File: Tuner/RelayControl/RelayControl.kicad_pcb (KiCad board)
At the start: 2 copper layers, 100 x 100 mm, 138 parts, among them J1 Conn_01x06, J12 Conn_01x01, J13 Conn_01x01, J14 Conn_01x01, J15 Conn_01x01, J2 Conn_02x16_Odd_Even, J3 Conn_01x06, J4 Conn_02x16_Odd_Even, J5 Conn_01x01, J6 Conn_01x01, J7 Conn_01x01, J8 Conn_01x01, U1 MCP23017, U2 ULN2803A, U3 ULN2803A, U4 MCP23017, U5 ULN2803A, U6 ULN2803A

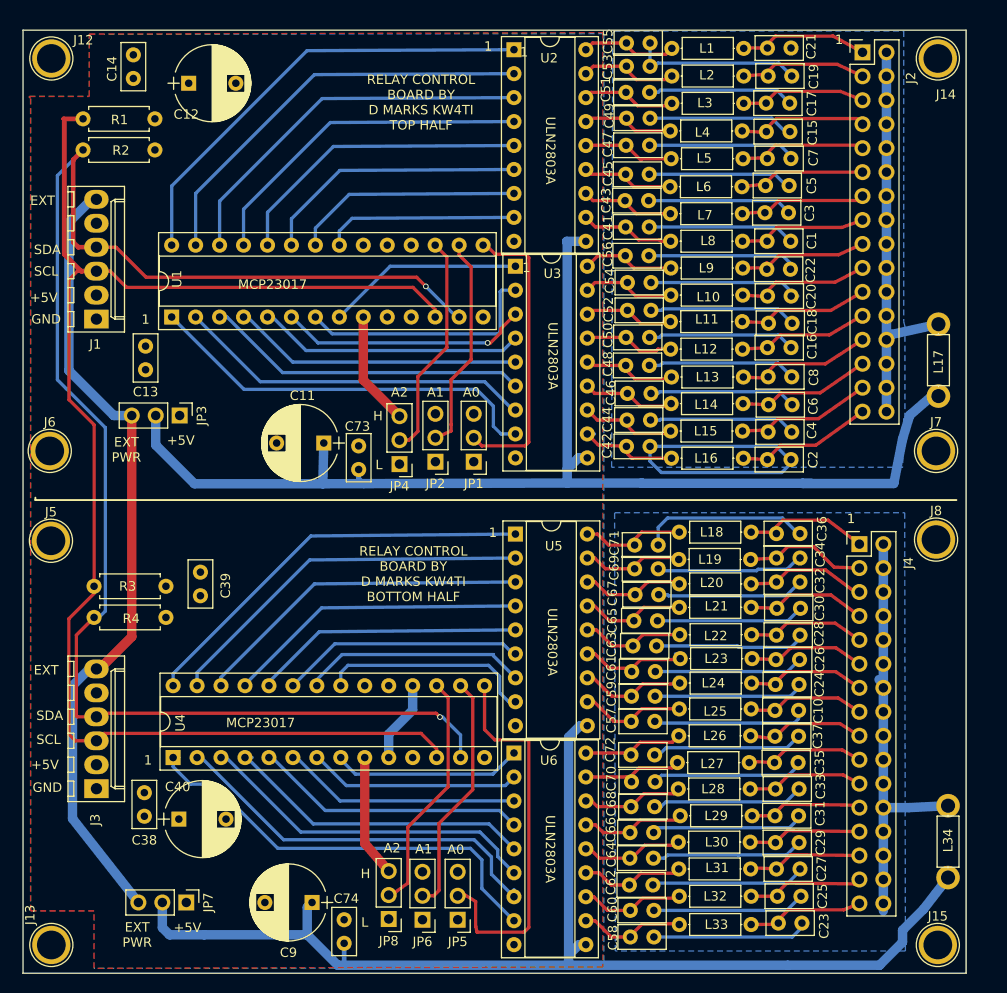
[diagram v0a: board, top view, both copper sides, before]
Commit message: Modified RelayControl and Reversible Section to Isolate Digital from Analog sections using RF chokes
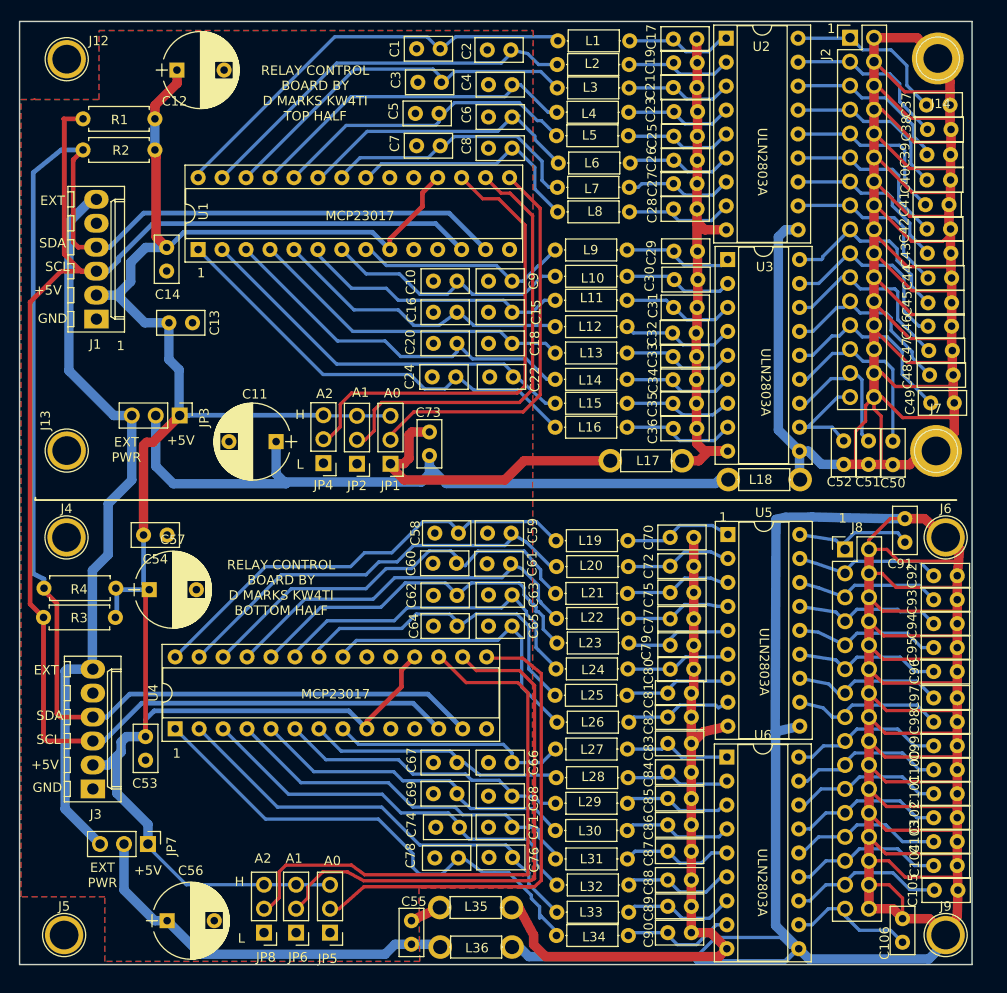
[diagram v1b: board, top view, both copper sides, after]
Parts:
- removed J15: Conn_01x01, Connectors:1pin
- added C100: 10 nF, Capacitors_THT:C_Disc_D5.0mm_W2.5mm_P2.50mm, F.Cu at (146.6, 128.4)
- added C101: 10 nF, Capacitors_THT:C_Disc_D5.0mm_W2.5mm_P2.50mm, F.Cu at (146.6, 131.0)
- added C102: 10 nF, Capacitors_THT:C_Disc_D5.0mm_W2.5mm_P2.50mm, F.Cu at (146.6, 133.5)
- added C103: 10 nF, Capacitors_THT:C_Disc_D5.0mm_W2.5mm_P2.50mm, F.Cu at (146.6, 136.0)
- added C104: 10 nF, Capacitors_THT:C_Disc_D5.0mm_W2.5mm_P2.50mm, F.Cu at (146.6, 138.6)
- added C105: 10 nF, Capacitors_THT:C_Disc_D5.0mm_W2.5mm_P2.50mm, F.Cu at (146.6, 141.2)
- added C106: 10 nF, Capacitors_THT:C_Disc_D5.0mm_W2.5mm_P2.50mm, F.Cu at (143.3, 146.7)
- added C75: 10 nF, Capacitors_THT:C_Disc_D5.0mm_W2.5mm_P2.50mm, F.Cu at (118.6, 109.6)
- added C76: 10 nF, Capacitors_THT:C_Disc_D5.0mm_W2.5mm_P2.50mm, F.Cu at (101.9, 137.7)
- added C77: 10 nF, Capacitors_THT:C_Disc_D5.0mm_W2.5mm_P2.50mm, F.Cu at (118.6, 112.4)
- added C78: 10 nF, Capacitors_THT:C_Disc_D5.0mm_W2.5mm_P2.50mm, F.Cu at (96.2, 137.8)
- added C79: 10 nF, Capacitors_THT:C_Disc_D5.0mm_W2.5mm_P2.50mm, F.Cu at (118.6, 115.2)
- added C80: 10 nF, Capacitors_THT:C_Disc_D5.0mm_W2.5mm_P2.50mm, F.Cu at (118.6, 117.8)
- added C81: 10 nF, Capacitors_THT:C_Disc_D5.0mm_W2.5mm_P2.50mm, F.Cu at (118.4, 120.3)
- added C82: 10 nF, Capacitors_THT:C_Disc_D5.0mm_W2.5mm_P2.50mm, F.Cu at (118.4, 122.8)
- added C83: 10 nF, Capacitors_THT:C_Disc_D5.0mm_W2.5mm_P2.50mm, F.Cu at (118.4, 125.6)
- added C84: 10 nF, Capacitors_THT:C_Disc_D5.0mm_W2.5mm_P2.50mm, F.Cu at (118.4, 128.7)
- added C85: 10 nF, Capacitors_THT:C_Disc_D5.0mm_W2.5mm_P2.50mm, F.Cu at (118.4, 131.5)
- added C86: 10 nF, Capacitors_THT:C_Disc_D5.0mm_W2.5mm_P2.50mm, F.Cu at (118.4, 134.3)
- added C87: 10 nF, Capacitors_THT:C_Disc_D5.0mm_W2.5mm_P2.50mm, F.Cu at (118.4, 137.1)
- added C88: 10 nF, Capacitors_THT:C_Disc_D5.0mm_W2.5mm_P2.50mm, F.Cu at (118.4, 140.1)
- added C89: 10 nF, Capacitors_THT:C_Disc_D5.0mm_W2.5mm_P2.50mm, F.Cu at (118.4, 142.9)
- added C90: 10 nF, Capacitors_THT:C_Disc_D5.0mm_W2.5mm_P2.50mm, F.Cu at (118.4, 145.7)
- added C91: 10 nF, Capacitors_THT:C_Disc_D5.0mm_W2.5mm_P2.50mm, F.Cu at (143.5, 104.3)
- added C92: 10 nF, Capacitors_THT:C_Disc_D5.0mm_W2.5mm_P2.50mm, F.Cu at (146.6, 107.8)
- added C93: 10 nF, Capacitors_THT:C_Disc_D5.0mm_W2.5mm_P2.50mm, F.Cu at (146.6, 110.4)
- added C94: 10 nF, Capacitors_THT:C_Disc_D5.0mm_W2.5mm_P2.50mm, F.Cu at (146.6, 112.9)
- added C95: 10 nF, Capacitors_THT:C_Disc_D5.0mm_W2.5mm_P2.50mm, F.Cu at (146.6, 115.5)
- added C96: 10 nF, Capacitors_THT:C_Disc_D5.0mm_W2.5mm_P2.50mm, F.Cu at (146.6, 118.0)
- added C97: 10 nF, Capacitors_THT:C_Disc_D5.0mm_W2.5mm_P2.50mm, F.Cu at (146.6, 120.8)
- added C98: 10 nF, Capacitors_THT:C_Disc_D5.0mm_W2.5mm_P2.50mm, F.Cu at (146.6, 123.3)
- added C99: 10 nF, Capacitors_THT:C_Disc_D5.0mm_W2.5mm_P2.50mm, F.Cu at (146.6, 125.9)
- added J9: Conn_01x01, Connectors:1pin, F.Cu at (147.8, 145.9)
- added L35: 100 uH, Inductors_THT:L_Axial_L5.3mm_D2.2mm_P7.62mm_Horizontal_Vishay_IM-1, F.Cu at (94.2, 143.0)
- added L36: 100 uH, Inductors_THT:L_Axial_L5.3mm_D2.2mm_P7.62mm_Horizontal_Vishay_IM-1, F.Cu at (101.9, 147.2)
- C38, C39, C74: value 100 nF -> 10 nF
- C40, C9: value 100 uF -> 10 nF; footprint Capacitors_THT:CP_Radial_D8.0mm_P5.00mm -> Capacitors_THT:C_Disc_D5.0mm_W2.5mm_P2.50mm
- C53, C54, C55: value 10 nF -> 100 nF
- C56, C57: value 10 nF -> 100 uF; footprint Capacitors_THT:C_Disc_D5.0mm_W2.5mm_P2.50mm -> Capacitors_THT:CP_Radial_D8.0mm_P5.00mm
- J4: value Conn_02x16_Odd_Even -> Conn_01x01; footprint Pin_Headers:Pin_Header_Straight_2x16_Pitch2.54mm -> Connectors:1pin
- J8: value Conn_01x01 -> Conn_02x16_Odd_Even; footprint Connectors:1pin -> Pin_Headers:Pin_Header_Straight_2x16_Pitch2.54mm
- moved C38 110.4 mm to (145.9, 60.5), turned to 0 degrees
- moved C40 104.3 mm to (145.8, 65.9)
- moved C55 96.4 mm to (91.2, 144.4), turned to 270 degrees
- moved J6 95.4 mm to (147.8, 103.8)
- moved C53 91.0 mm to (63.0, 127.4), turned to 90 degrees
- moved C39 90.1 mm to (145.8, 63.2), turned to 0 degrees
- moved C23 87.1 mm to (119.0, 58.6), turned to 0 degrees
- moved C56 87.1 mm to (65.3, 144.4), turned to 0 degrees
- moved J4 84.1 mm to (54.6, 103.8)
- moved C25 81.7 mm to (119.0, 61.2), turned to 0 degrees
- moved C27 73.9 mm to (119.0, 66.3), turned to 0 degrees
- moved C9 69.2 mm to (101.9, 76.6)
- moved C37 68.3 mm to (145.8, 57.9), turned to 0 degrees
- moved C29 64.1 mm to (119.0, 73.4), turned to 0 degrees
- moved C10 58.2 mm to (96.0, 76.6)
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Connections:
- C1 pad 2: Net-(C1-Pad2) -> GND
- C10 pad 2: Net-(C10-Pad2) -> GND
- C15 pad 1: Net-(C1-Pad1) -> Net-(C15-Pad1)
- C15 pad 2: Net-(C15-Pad2) -> GND
- C16 pad 1: Net-(C1-Pad1) -> Net-(C16-Pad1)
- C16 pad 2: Net-(C16-Pad2) -> GND
- C17 pad 1: Net-(C1-Pad1) -> Net-(C17-Pad1)
- C18 pad 1: Net-(C1-Pad1) -> Net-(C18-Pad1)
- C18 pad 2: Net-(C18-Pad2) -> GND
- C19 pad 1: Net-(C1-Pad1) -> Net-(C19-Pad1)
- C19 pad 2: Net-(C19-Pad2) -> Net-(C17-Pad2)
- C2 pad 1: Net-(C1-Pad1) -> Net-(C2-Pad1)
- C2 pad 2: Net-(C2-Pad2) -> GND
- C20 pad 1: Net-(C1-Pad1) -> Net-(C20-Pad1)
- C20 pad 2: Net-(C20-Pad2) -> GND
- C21 pad 1: Net-(C1-Pad1) -> Net-(C21-Pad1)
- C21 pad 2: Net-(C21-Pad2) -> Net-(C17-Pad2)
- C22 pad 1: Net-(C1-Pad1) -> Net-(C22-Pad1)
- C22 pad 2: Net-(C22-Pad2) -> GND
- C23 pad 1: Net-(C10-Pad1) -> Net-(C23-Pad1)
- C23 pad 2: Net-(C23-Pad2) -> Net-(C17-Pad2)
- C24 pad 1: Net-(C10-Pad1) -> Net-(C24-Pad1)
- C24 pad 2: Net-(C24-Pad2) -> GND
- C25 pad 1: Net-(C10-Pad1) -> Net-(C25-Pad1)
- C25 pad 2: Net-(C25-Pad2) -> Net-(C17-Pad2)
- C26 pad 1: Net-(C10-Pad1) -> Net-(C26-Pad1)
- C26 pad 2: Net-(C26-Pad2) -> Net-(C17-Pad2)
- C27 pad 1: Net-(C10-Pad1) -> Net-(C27-Pad1)
- C27 pad 2: Net-(C27-Pad2) -> Net-(C17-Pad2)
- C28 pad 1: Net-(C10-Pad1) -> Net-(C28-Pad1)
- C28 pad 2: Net-(C28-Pad2) -> Net-(C17-Pad2)
- C29 pad 1: Net-(C10-Pad1) -> Net-(C29-Pad1)
- C29 pad 2: Net-(C29-Pad2) -> Net-(C17-Pad2)
- C3 pad 1: Net-(C1-Pad1) -> Net-(C3-Pad1)
- C3 pad 2: Net-(C3-Pad2) -> GND
- C30 pad 1: Net-(C10-Pad1) -> Net-(C30-Pad1)
- C30 pad 2: Net-(C30-Pad2) -> Net-(C17-Pad2)
- C31 pad 1: Net-(C10-Pad1) -> Net-(C31-Pad1)
- C31 pad 2: Net-(C31-Pad2) -> Net-(C17-Pad2)
- C32 pad 1: Net-(C10-Pad1) -> Net-(C32-Pad1)
- C32 pad 2: Net-(C32-Pad2) -> Net-(C17-Pad2)
- C33 pad 1: Net-(C10-Pad1) -> Net-(C33-Pad1)
- C33 pad 2: Net-(C33-Pad2) -> Net-(C17-Pad2)
- C34 pad 1: Net-(C10-Pad1) -> Net-(C34-Pad1)
- C34 pad 2: Net-(C34-Pad2) -> Net-(C17-Pad2)
- C35 pad 1: Net-(C10-Pad1) -> Net-(C35-Pad1)
- C35 pad 2: Net-(C35-Pad2) -> Net-(C17-Pad2)
- C36 pad 1: Net-(C10-Pad1) -> Net-(C36-Pad1)
- C36 pad 2: Net-(C36-Pad2) -> Net-(C17-Pad2)
- C37 pad 1: Net-(C10-Pad1) -> Net-(C37-Pad1)
- C38 pad 1: GND -> Net-(C38-Pad1)
- C38 pad 2: +5V -> Net-(C37-Pad2)
- C39 pad 1: GND -> Net-(C39-Pad1)
- C39 pad 2: +5V -> Net-(C37-Pad2)
- C4 pad 1: Net-(C1-Pad1) -> Net-(C4-Pad1)
- C4 pad 2: Net-(C4-Pad2) -> GND
- C40 pad 1: +5V -> Net-(C40-Pad1)
- C40 pad 2: GND -> Net-(C37-Pad2)
- C41 pad 1: Net-(C1-Pad1) -> Net-(C41-Pad1)
- C41 pad 2: Net-(C41-Pad2) -> Net-(C37-Pad2)
- C42 pad 1: Net-(C1-Pad1) -> Net-(C42-Pad1)
- C42 pad 2: Net-(C42-Pad2) -> Net-(C37-Pad2)
- C43 pad 1: Net-(C1-Pad1) -> Net-(C43-Pad1)
- C43 pad 2: Net-(C43-Pad2) -> Net-(C37-Pad2)
- C44 pad 1: Net-(C1-Pad1) -> Net-(C44-Pad1)
- C44 pad 2: Net-(C44-Pad2) -> Net-(C37-Pad2)
- C45 pad 1: Net-(C1-Pad1) -> Net-(C45-Pad1)
- C45 pad 2: Net-(C45-Pad2) -> Net-(C37-Pad2)
- C46 pad 1: Net-(C1-Pad1) -> Net-(C46-Pad1)
- C46 pad 2: Net-(C46-Pad2) -> Net-(C37-Pad2)
- C47 pad 1: Net-(C1-Pad1) -> Net-(C47-Pad1)
- C47 pad 2: Net-(C47-Pad2) -> Net-(C37-Pad2)
- C48 pad 1: Net-(C1-Pad1) -> Net-(C48-Pad1)
- C48 pad 2: Net-(C48-Pad2) -> Net-(C37-Pad2)
- C49 pad 1: Net-(C1-Pad1) -> Net-(C49-Pad1)
- C49 pad 2: Net-(C49-Pad2) -> Net-(C37-Pad2)
- C5 pad 1: Net-(C1-Pad1) -> Net-(C5-Pad1)
- C5 pad 2: Net-(C5-Pad2) -> GND
- C50 pad 1: Net-(C1-Pad1) -> Net-(C50-Pad1)
- C50 pad 2: Net-(C50-Pad2) -> Net-(C37-Pad2)
- C51 pad 1: Net-(C1-Pad1) -> Net-(C51-Pad1)
- C51 pad 2: Net-(C51-Pad2) -> Net-(C37-Pad2)
- C52 pad 1: Net-(C1-Pad1) -> Net-(C52-Pad1)
- C52 pad 2: Net-(C52-Pad2) -> Net-(C37-Pad2)
- C53 pad 1: Net-(C1-Pad1) -> GND
- C53 pad 2: Net-(C53-Pad2) -> +5V
- C54 pad 1: Net-(C1-Pad1) -> GND
- C54 pad 2: Net-(C54-Pad2) -> +5V
- C55 pad 1: Net-(C1-Pad1) -> GND
- C55 pad 2: Net-(C55-Pad2) -> RLYPWR2
- C56 pad 1: Net-(C1-Pad1) -> RLYPWR2
- C56 pad 2: Net-(C56-Pad2) -> GND
- C57 pad 1: Net-(C10-Pad1) -> +5V
- C57 pad 2: Net-(C57-Pad2) -> GND
- C58 pad 1: Net-(C10-Pad1) -> Net-(C58-Pad1)
- C58 pad 2: Net-(C58-Pad2) -> GND
- C59 pad 1: Net-(C10-Pad1) -> Net-(C59-Pad1)
- C59 pad 2: Net-(C59-Pad2) -> GND
- C6 pad 1: Net-(C1-Pad1) -> Net-(C6-Pad1)
- C6 pad 2: Net-(C6-Pad2) -> GND
- C60 pad 1: Net-(C10-Pad1) -> Net-(C60-Pad1)
- C60 pad 2: Net-(C60-Pad2) -> GND
- C61 pad 1: Net-(C10-Pad1) -> Net-(C61-Pad1)
- C61 pad 2: Net-(C61-Pad2) -> GND
- C62 pad 1: Net-(C10-Pad1) -> Net-(C62-Pad1)
- C62 pad 2: Net-(C62-Pad2) -> GND
- C63 pad 1: Net-(C10-Pad1) -> Net-(C63-Pad1)
- C63 pad 2: Net-(C63-Pad2) -> GND
- C64 pad 1: Net-(C10-Pad1) -> Net-(C64-Pad1)
- C64 pad 2: Net-(C64-Pad2) -> GND
- C65 pad 1: Net-(C10-Pad1) -> Net-(C65-Pad1)
- C65 pad 2: Net-(C65-Pad2) -> GND
- C66 pad 1: Net-(C10-Pad1) -> Net-(C66-Pad1)
- C66 pad 2: Net-(C66-Pad2) -> GND
- C67 pad 1: Net-(C10-Pad1) -> Net-(C67-Pad1)
- C67 pad 2: Net-(C67-Pad2) -> GND
- C68 pad 1: Net-(C10-Pad1) -> Net-(C68-Pad1)
- C68 pad 2: Net-(C68-Pad2) -> GND
- C69 pad 1: Net-(C10-Pad1) -> Net-(C69-Pad1)
- C69 pad 2: Net-(C69-Pad2) -> GND
- C7 pad 1: Net-(C1-Pad1) -> Net-(C7-Pad1)
- C7 pad 2: Net-(C7-Pad2) -> GND
- C70 pad 1: Net-(C10-Pad1) -> Net-(C70-Pad1)
- C71 pad 1: Net-(C10-Pad1) -> Net-(C71-Pad1)
- C71 pad 2: Net-(C71-Pad2) -> GND
- C72 pad 1: Net-(C10-Pad1) -> Net-(C72-Pad1)
- C72 pad 2: Net-(C72-Pad2) -> Net-(C70-Pad2)
- C74 pad 1: GND -> Net-(C74-Pad1)
- C74 pad 2: RLYPWR2 -> GND
- C8 pad 1: Net-(C1-Pad1) -> Net-(C8-Pad1)
- C8 pad 2: Net-(C8-Pad2) -> GND
- C9 pad 1: RLYPWR2 -> Net-(C9-Pad1)
- J14 pad 1: (no net) -> Net-(C37-Pad2)
- J2 pad 1: Net-(C21-Pad2) -> Net-(C37-Pad1)
- J2 pad 10: Net-(C1-Pad1) -> Net-(C37-Pad2)
- J2 pad 11: Net-(C5-Pad2) -> Net-(C42-Pad1)
- J2 pad 12: Net-(C1-Pad1) -> Net-(C37-Pad2)
- J2 pad 13: Net-(C3-Pad2) -> Net-(C43-Pad1)
- J2 pad 14: Net-(C1-Pad1) -> Net-(C37-Pad2)
- J2 pad 15: Net-(C1-Pad2) -> Net-(C44-Pad1)
- J2 pad 16: Net-(C1-Pad1) -> Net-(C37-Pad2)
- J2 pad 17: Net-(C22-Pad2) -> Net-(C45-Pad1)
- J2 pad 18: Net-(C1-Pad1) -> Net-(C37-Pad2)
- J2 pad 19: Net-(C20-Pad2) -> Net-(C46-Pad1)
- J2 pad 2: Net-(C1-Pad1) -> Net-(C37-Pad2)
- J2 pad 20: Net-(C1-Pad1) -> Net-(C37-Pad2)
- J2 pad 21: Net-(C18-Pad2) -> Net-(C47-Pad1)
- J2 pad 22: Net-(C1-Pad1) -> Net-(C37-Pad2)
- J2 pad 23: Net-(C16-Pad2) -> Net-(C48-Pad1)
- J2 pad 24: Net-(C1-Pad1) -> Net-(C37-Pad2)
- J2 pad 25: Net-(C8-Pad2) -> Net-(C49-Pad1)
- J2 pad 26: Net-(C1-Pad1) -> Net-(C37-Pad2)
- J2 pad 27: Net-(C6-Pad2) -> Net-(C50-Pad1)
- J2 pad 28: Net-(C1-Pad1) -> Net-(C37-Pad2)
- J2 pad 29: Net-(C4-Pad2) -> Net-(C51-Pad1)
- J2 pad 3: Net-(C19-Pad2) -> Net-(C38-Pad1)
- J2 pad 30: Net-(C1-Pad1) -> Net-(C37-Pad2)
- J2 pad 31: Net-(C2-Pad2) -> Net-(C52-Pad1)
- J2 pad 32: Net-(C1-Pad1) -> Net-(C37-Pad2)
- J2 pad 4: Net-(C1-Pad1) -> Net-(C37-Pad2)
- J2 pad 5: Net-(C17-Pad2) -> Net-(C39-Pad1)
- J2 pad 6: Net-(C1-Pad1) -> Net-(C37-Pad2)
- J2 pad 7: Net-(C15-Pad2) -> Net-(C40-Pad1)
- J2 pad 8: Net-(C1-Pad1) -> Net-(C37-Pad2)
- J2 pad 9: Net-(C7-Pad2) -> Net-(C41-Pad1)
- J4 pad 1: Net-(C36-Pad2) -> (no net)
- J6 pad 1: (no net) -> Net-(C100-Pad2)
- J7 pad 1: (no net) -> Net-(C37-Pad2)
- J8 pad 1: (no net) -> Net-(C91-Pad1)
- L1 pad 1: Net-(C21-Pad2) -> Net-(C17-Pad1)
- L1 pad 2: Net-(C55-Pad2) -> Net-(C1-Pad1)
- L10 pad 1: Net-(C20-Pad2) -> Net-(C30-Pad1)
- L10 pad 2: Net-(C54-Pad2) -> Net-(C10-Pad1)
- L11 pad 1: Net-(C18-Pad2) -> Net-(C31-Pad1)
- L11 pad 2: Net-(C52-Pad2) -> Net-(C15-Pad1)
- L12 pad 1: Net-(C16-Pad2) -> Net-(C32-Pad1)
- L12 pad 2: Net-(C50-Pad2) -> Net-(C16-Pad1)
- L13 pad 1: Net-(C8-Pad2) -> Net-(C33-Pad1)
- L13 pad 2: Net-(C48-Pad2) -> Net-(C18-Pad1)
- L14 pad 1: Net-(C6-Pad2) -> Net-(C34-Pad1)
- L14 pad 2: Net-(C46-Pad2) -> Net-(C20-Pad1)
- L15 pad 1: Net-(C4-Pad2) -> Net-(C35-Pad1)
- L15 pad 2: Net-(C44-Pad2) -> Net-(C22-Pad1)
- L16 pad 1: Net-(C2-Pad2) -> Net-(C36-Pad1)
- L16 pad 2: Net-(C42-Pad2) -> Net-(C24-Pad1)
- L17 pad 1: Net-(C1-Pad1) -> GND
- L17 pad 2: RLYPWR -> Net-(C17-Pad2)
- L18 pad 1: Net-(C36-Pad2) -> Net-(C37-Pad2)
- L18 pad 2: Net-(C71-Pad2) -> RLYPWR
- L19 pad 1: Net-(C34-Pad2) -> Net-(C70-Pad1)
- L19 pad 2: Net-(C69-Pad2) -> Net-(C58-Pad1)
- L2 pad 1: Net-(C19-Pad2) -> Net-(C19-Pad1)
- L2 pad 2: Net-(C53-Pad2) -> Net-(C2-Pad1)
- L20 pad 1: Net-(C32-Pad2) -> Net-(C72-Pad1)
- L20 pad 2: Net-(C67-Pad2) -> Net-(C59-Pad1)
- L21 pad 1: Net-(C30-Pad2) -> Net-(C75-Pad1)
- L21 pad 2: Net-(C65-Pad2) -> Net-(C60-Pad1)
- L22 pad 1: Net-(C28-Pad2) -> Net-(C77-Pad1)
- L22 pad 2: Net-(C63-Pad2) -> Net-(C61-Pad1)
- L23 pad 1: Net-(C26-Pad2) -> Net-(C79-Pad1)
- L23 pad 2: Net-(C61-Pad2) -> Net-(C62-Pad1)
- L24 pad 1: Net-(C24-Pad2) -> Net-(C80-Pad1)
- L24 pad 2: Net-(C59-Pad2) -> Net-(C63-Pad1)
- L25 pad 1: Net-(C10-Pad2) -> Net-(C81-Pad1)
- L25 pad 2: Net-(C57-Pad2) -> Net-(C64-Pad1)
- L26 pad 1: Net-(C37-Pad2) -> Net-(C82-Pad1)
- L26 pad 2: Net-(C72-Pad2) -> Net-(C65-Pad1)
- L27 pad 1: Net-(C35-Pad2) -> Net-(C83-Pad1)
- L27 pad 2: Net-(C70-Pad2) -> Net-(C66-Pad1)
- L28 pad 1: Net-(C33-Pad2) -> Net-(C84-Pad1)
- L28 pad 2: Net-(C68-Pad2) -> Net-(C67-Pad1)
- L29 pad 1: Net-(C31-Pad2) -> Net-(C85-Pad1)
- L29 pad 2: Net-(C66-Pad2) -> Net-(C68-Pad1)
- L3 pad 1: Net-(C17-Pad2) -> Net-(C21-Pad1)
- L3 pad 2: Net-(C51-Pad2) -> Net-(C3-Pad1)
- L30 pad 1: Net-(C29-Pad2) -> Net-(C86-Pad1)
- L30 pad 2: Net-(C64-Pad2) -> Net-(C69-Pad1)
- L31 pad 1: Net-(C27-Pad2) -> Net-(C87-Pad1)
- L31 pad 2: Net-(C62-Pad2) -> Net-(C71-Pad1)
- L32 pad 1: Net-(C25-Pad2) -> Net-(C88-Pad1)
- L32 pad 2: Net-(C60-Pad2) -> Net-(C74-Pad1)
- L33 pad 1: Net-(C23-Pad2) -> Net-(C89-Pad1)
- L33 pad 2: Net-(C58-Pad2) -> Net-(C76-Pad1)
- L34 pad 1: Net-(C10-Pad1) -> Net-(C90-Pad1)
- L34 pad 2: RLYPWR2 -> Net-(C78-Pad1)
- L4 pad 1: Net-(C15-Pad2) -> Net-(C23-Pad1)
- L4 pad 2: Net-(C49-Pad2) -> Net-(C4-Pad1)
- L5 pad 1: Net-(C7-Pad2) -> Net-(C25-Pad1)
- L5 pad 2: Net-(C47-Pad2) -> Net-(C5-Pad1)
- L6 pad 1: Net-(C5-Pad2) -> Net-(C26-Pad1)
- L6 pad 2: Net-(C45-Pad2) -> Net-(C6-Pad1)
- L7 pad 1: Net-(C3-Pad2) -> Net-(C27-Pad1)
- L7 pad 2: Net-(C43-Pad2) -> Net-(C7-Pad1)
- L8 pad 1: Net-(C1-Pad2) -> Net-(C28-Pad1)
- L8 pad 2: Net-(C41-Pad2) -> Net-(C8-Pad1)
- L9 pad 1: Net-(C22-Pad2) -> Net-(C29-Pad1)
- L9 pad 2: Net-(C56-Pad2) -> Net-(C9-Pad1)
- U1 pad 1: Net-(U1-Pad1) -> Net-(C24-Pad1)
- U1 pad 18: GND -> +5V
- U1 pad 2: Net-(U1-Pad2) -> Net-(C22-Pad1)
- U1 pad 21: Net-(U1-Pad21) -> Net-(C8-Pad1)
- U1 pad 22: Net-(U1-Pad22) -> Net-(C7-Pad1)
- U1 pad 23: Net-(U1-Pad23) -> Net-(C6-Pad1)
- U1 pad 24: Net-(U1-Pad24) -> Net-(C5-Pad1)
- U1 pad 25: Net-(U1-Pad25) -> Net-(C4-Pad1)
- U1 pad 26: Net-(U1-Pad26) -> Net-(C3-Pad1)
- U1 pad 27: Net-(U1-Pad27) -> Net-(C2-Pad1)
- U1 pad 28: Net-(U1-Pad28) -> Net-(C1-Pad1)
- U1 pad 3: Net-(U1-Pad3) -> Net-(C20-Pad1)
- U1 pad 4: Net-(U1-Pad4) -> Net-(C18-Pad1)
- U1 pad 5: Net-(U1-Pad5) -> Net-(C16-Pad1)
- U1 pad 6: Net-(U1-Pad6) -> Net-(C15-Pad1)
- U1 pad 7: Net-(U1-Pad7) -> Net-(C10-Pad1)
- U1 pad 8: Net-(U1-Pad8) -> Net-(C9-Pad1)
- U2 pad 1: Net-(U1-Pad28) -> Net-(C17-Pad1)
- U2 pad 10: RLYPWR -> Net-(C37-Pad2)
- U2 pad 11: Net-(C41-Pad2) -> Net-(C44-Pad1)
- U2 pad 12: Net-(C43-Pad2) -> Net-(C43-Pad1)
- U2 pad 13: Net-(C45-Pad2) -> Net-(C42-Pad1)
- U2 pad 14: Net-(C47-Pad2) -> Net-(C41-Pad1)
- U2 pad 15: Net-(C49-Pad2) -> Net-(C40-Pad1)
- U2 pad 16: Net-(C51-Pad2) -> Net-(C39-Pad1)
- U2 pad 17: Net-(C53-Pad2) -> Net-(C38-Pad1)
- U2 pad 18: Net-(C55-Pad2) -> Net-(C37-Pad1)
- U2 pad 2: Net-(U1-Pad27) -> Net-(C19-Pad1)
- U2 pad 3: Net-(U1-Pad26) -> Net-(C21-Pad1)
- U2 pad 4: Net-(U1-Pad25) -> Net-(C23-Pad1)
- U2 pad 5: Net-(U1-Pad24) -> Net-(C25-Pad1)
- U2 pad 6: Net-(U1-Pad23) -> Net-(C26-Pad1)
- U2 pad 7: Net-(U1-Pad22) -> Net-(C27-Pad1)
- U2 pad 8: Net-(U1-Pad21) -> Net-(C28-Pad1)
- U2 pad 9: GND -> Net-(C17-Pad2)
- U3 pad 1: Net-(U1-Pad8) -> Net-(C29-Pad1)
- U3 pad 10: RLYPWR -> Net-(C37-Pad2)
- U3 pad 11: Net-(C42-Pad2) -> Net-(C52-Pad1)
- U3 pad 12: Net-(C44-Pad2) -> Net-(C51-Pad1)
- U3 pad 13: Net-(C46-Pad2) -> Net-(C50-Pad1)
- U3 pad 14: Net-(C48-Pad2) -> Net-(C49-Pad1)
- U3 pad 15: Net-(C50-Pad2) -> Net-(C48-Pad1)
- U3 pad 16: Net-(C52-Pad2) -> Net-(C47-Pad1)
- U3 pad 17: Net-(C54-Pad2) -> Net-(C46-Pad1)
- U3 pad 18: Net-(C56-Pad2) -> Net-(C45-Pad1)
- U3 pad 2: Net-(U1-Pad7) -> Net-(C30-Pad1)
- U3 pad 3: Net-(U1-Pad6) -> Net-(C31-Pad1)
- U3 pad 4: Net-(U1-Pad5) -> Net-(C32-Pad1)
- U3 pad 5: Net-(U1-Pad4) -> Net-(C33-Pad1)
- U3 pad 6: Net-(U1-Pad3) -> Net-(C34-Pad1)
- U3 pad 7: Net-(U1-Pad2) -> Net-(C35-Pad1)
- U3 pad 8: Net-(U1-Pad1) -> Net-(C36-Pad1)
- U3 pad 9: GND -> Net-(C17-Pad2)
- U4 pad 1: Net-(U4-Pad1) -> Net-(C78-Pad1)
- U4 pad 18: GND -> +5V
- U4 pad 2: Net-(U4-Pad2) -> Net-(C76-Pad1)
- U4 pad 21: Net-(U4-Pad21) -> Net-(C65-Pad1)
- U4 pad 22: Net-(U4-Pad22) -> Net-(C64-Pad1)
- U4 pad 23: Net-(U4-Pad23) -> Net-(C63-Pad1)
- U4 pad 24: Net-(U4-Pad24) -> Net-(C62-Pad1)
- U4 pad 25: Net-(U4-Pad25) -> Net-(C61-Pad1)
- U4 pad 26: Net-(U4-Pad26) -> Net-(C60-Pad1)
- U4 pad 27: Net-(U4-Pad27) -> Net-(C59-Pad1)
- U4 pad 28: Net-(U4-Pad28) -> Net-(C58-Pad1)
- U4 pad 3: Net-(U4-Pad3) -> Net-(C74-Pad1)
- U4 pad 4: Net-(U4-Pad4) -> Net-(C71-Pad1)
- U4 pad 5: Net-(U4-Pad5) -> Net-(C69-Pad1)
- U4 pad 6: Net-(U4-Pad6) -> Net-(C68-Pad1)
- U4 pad 7: Net-(U4-Pad7) -> Net-(C67-Pad1)
- U4 pad 8: Net-(U4-Pad8) -> Net-(C66-Pad1)
- U5 pad 1: Net-(U4-Pad28) -> Net-(C70-Pad1)
- U5 pad 10: RLYPWR2 -> Net-(C100-Pad2)
- U5 pad 11: Net-(C57-Pad2) -> Net-(C98-Pad1)
- U5 pad 12: Net-(C59-Pad2) -> Net-(C97-Pad1)
- U5 pad 13: Net-(C61-Pad2) -> Net-(C96-Pad1)
- U5 pad 14: Net-(C63-Pad2) -> Net-(C95-Pad1)
- U5 pad 15: Net-(C65-Pad2) -> Net-(C94-Pad1)
- U5 pad 16: Net-(C67-Pad2) -> Net-(C93-Pad1)
- U5 pad 17: Net-(C69-Pad2) -> Net-(C92-Pad1)
- U5 pad 18: Net-(C71-Pad2) -> Net-(C91-Pad1)
- U5 pad 2: Net-(U4-Pad27) -> Net-(C72-Pad1)
- U5 pad 3: Net-(U4-Pad26) -> Net-(C75-Pad1)
- U5 pad 4: Net-(U4-Pad25) -> Net-(C77-Pad1)
- U5 pad 5: Net-(U4-Pad24) -> Net-(C79-Pad1)
- U5 pad 6: Net-(U4-Pad23) -> Net-(C80-Pad1)
- U5 pad 7: Net-(U4-Pad22) -> Net-(C81-Pad1)
- U5 pad 8: Net-(U4-Pad21) -> Net-(C82-Pad1)
- U5 pad 9: GND -> Net-(C70-Pad2)
- U6 pad 1: Net-(U4-Pad8) -> Net-(C83-Pad1)
- U6 pad 10: RLYPWR2 -> Net-(C100-Pad2)
- U6 pad 11: Net-(C58-Pad2) -> Net-(C106-Pad1)
- U6 pad 12: Net-(C60-Pad2) -> Net-(C105-Pad1)
- U6 pad 13: Net-(C62-Pad2) -> Net-(C104-Pad1)
- U6 pad 14: Net-(C64-Pad2) -> Net-(C103-Pad1)
- U6 pad 15: Net-(C66-Pad2) -> Net-(C102-Pad1)
- U6 pad 16: Net-(C68-Pad2) -> Net-(C101-Pad1)
- U6 pad 17: Net-(C70-Pad2) -> Net-(C100-Pad1)
- U6 pad 18: Net-(C72-Pad2) -> Net-(C99-Pad1)
- U6 pad 2: Net-(U4-Pad7) -> Net-(C84-Pad1)
- U6 pad 3: Net-(U4-Pad6) -> Net-(C85-Pad1)
- U6 pad 4: Net-(U4-Pad5) -> Net-(C86-Pad1)
- U6 pad 5: Net-(U4-Pad4) -> Net-(C87-Pad1)
- U6 pad 6: Net-(U4-Pad3) -> Net-(C88-Pad1)
- U6 pad 7: Net-(U4-Pad2) -> Net-(C89-Pad1)
- U6 pad 8: Net-(U4-Pad1) -> Net-(C90-Pad1)
- U6 pad 9: GND -> Net-(C70-Pad2)
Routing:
- net Net-(C100-Pad2): track 0.00 -> 373.7 mm
- net Net-(C10-Pad1): track 310.6 -> 26.8 mm
- net Net-(C37-Pad2): track 12.8 -> 287.1 mm
- net Net-(C1-Pad1): track 304.7 -> 45.8 mm
- net +5V: track 25.1 -> 224.4 mm
- net RLYPWR2: track 127.6 -> 41.8 mm
- net Net-(C70-Pad2): track 11.1 -> 77.6 mm
- net RLYPWR: track 131.7 -> 75.1 mm
- net Net-(C78-Pad1): track 0.00 -> 53.4 mm
- net Net-(C58-Pad1): track 0.00 -> 48.9 mm
- net Net-(U1-Pad28): track 48.5 -> 0.00 mm
- net Net-(C76-Pad1): track 0.00 -> 47.1 mm
- net Net-(C24-Pad1): track 0.00 -> 46.8 mm
- net Net-(U4-Pad1): track 46.3 -> 0.00 mm
- net Net-(C59-Pad1): track 0.00 -> 45.1 mm
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- added copper zone on B.Cu, net GND
- removed copper zone on B.Cu, net +5V
- removed copper zone on B.Cu, net Net-(C1-Pad1)
- removed copper zone on B.Cu, net Net-(C10-Pad1)
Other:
- board size 100 x 100 mm -> 101 x 100 mm

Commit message: Added extra filtering and shunt to RF ground
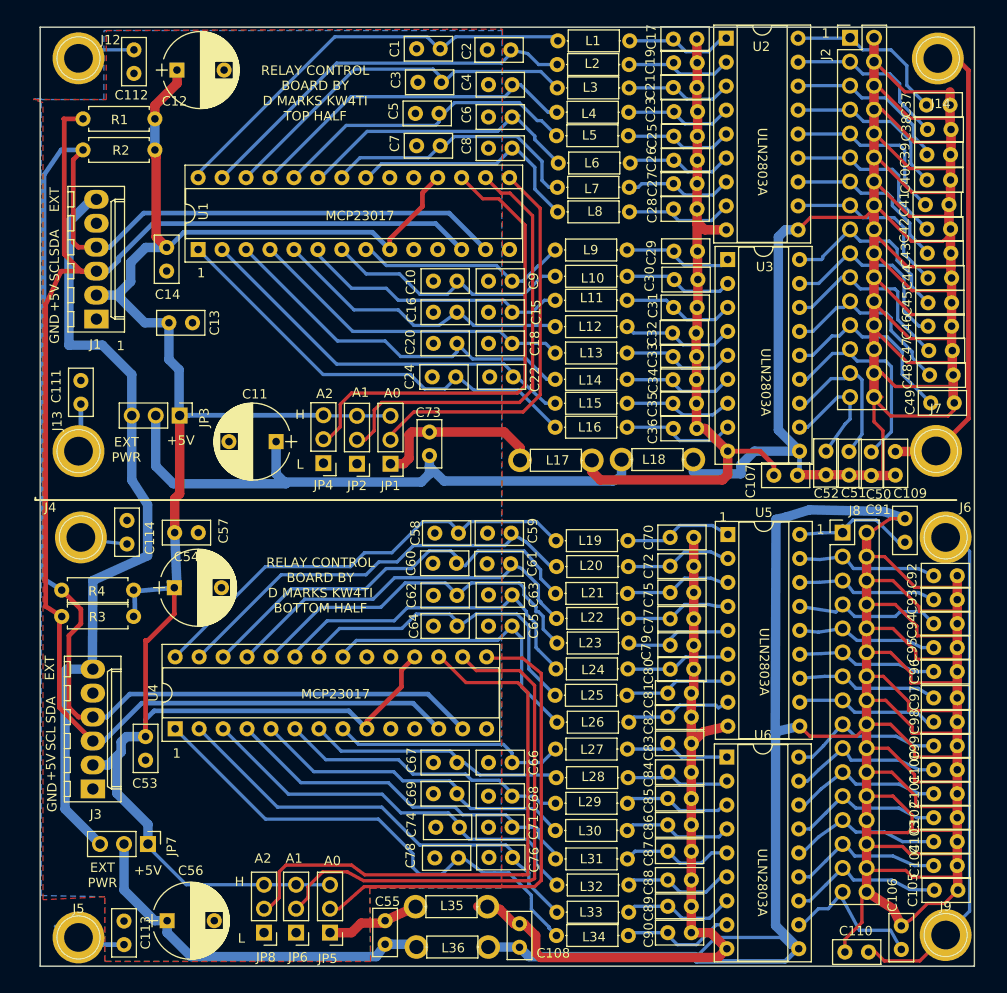
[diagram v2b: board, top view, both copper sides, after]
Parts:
- added C107: 10 nF, Capacitors_THT:C_Disc_D5.0mm_W2.5mm_P2.50mm, F.Cu at (129.6, 97.2)
- added C108: 10 nF, Capacitors_THT:C_Disc_D5.0mm_W2.5mm_P2.50mm, F.Cu at (102.6, 144.7)
- added C109: 10 nF, Capacitors_THT:C_Disc_D5.0mm_W2.5mm_P2.50mm, F.Cu at (142.5, 97.2)
- added C110: 10 nF, Capacitors_THT:C_Disc_D5.0mm_W2.5mm_P2.50mm, F.Cu at (139.6, 147.8)
- added C111: 10 nF, Capacitors_THT:C_Disc_D5.0mm_W2.5mm_P2.50mm, F.Cu at (56.1, 87.1)
- added C112: 10 nF, Capacitors_THT:C_Disc_D5.0mm_W2.5mm_P2.50mm, F.Cu at (61.8, 54.6)
- added C113: 10 nF, Capacitors_THT:C_Disc_D5.0mm_W2.5mm_P2.50mm, F.Cu at (60.7, 147.0)
- added C114: 10 nF, Capacitors_THT:C_Disc_D5.0mm_W2.5mm_P2.50mm, F.Cu at (61.0, 104.5)
- moved L18 11.5 mm to (121.1, 95.5)
- moved L17 9.58 mm to (102.7, 95.6)
- moved C54 3.31 mm to (68.6, 103.3)
- moved C55 2.79 mm to (88.4, 144.4)
- moved C57 2.67 mm to (66.0, 109.1)
- moved L35 2.57 mm to (91.6, 142.9)
- moved C50 2.55 mm to (139.9, 94.7)
- moved L36 2.52 mm to (99.3, 147.2)
- moved C51 2.36 mm to (137.6, 94.7)
- moved C52 2.17 mm to (135.1, 94.6)
- moved R3 1.93 mm to (61.7, 112.2)
- moved R4 1.89 mm to (61.7, 109.4)
- moved J8 1.80 mm to (136.9, 103.3)
- moved J5 1.55 mm to (55.9, 146.2)
- moved J4 1.52 mm to (56.1, 103.8)
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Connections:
- C37 pad 2: Net-(C37-Pad2) -> Net-(C107-Pad2)
- C38 pad 2: Net-(C37-Pad2) -> Net-(C107-Pad2)
- C39 pad 2: Net-(C37-Pad2) -> Net-(C107-Pad2)
- C40 pad 2: Net-(C37-Pad2) -> Net-(C107-Pad2)
- C41 pad 2: Net-(C37-Pad2) -> Net-(C107-Pad2)
- C42 pad 2: Net-(C37-Pad2) -> Net-(C107-Pad2)
- C43 pad 2: Net-(C37-Pad2) -> Net-(C107-Pad2)
- C44 pad 2: Net-(C37-Pad2) -> Net-(C107-Pad2)
- C45 pad 2: Net-(C37-Pad2) -> Net-(C107-Pad2)
- C46 pad 2: Net-(C37-Pad2) -> Net-(C107-Pad2)
- C47 pad 2: Net-(C37-Pad2) -> Net-(C107-Pad2)
- C48 pad 2: Net-(C37-Pad2) -> Net-(C107-Pad2)
- C49 pad 2: Net-(C37-Pad2) -> Net-(C107-Pad2)
- C50 pad 2: Net-(C37-Pad2) -> Net-(C107-Pad2)
- C51 pad 2: Net-(C37-Pad2) -> Net-(C107-Pad2)
- C52 pad 2: Net-(C37-Pad2) -> Net-(C107-Pad2)
- J12 pad 1: (no net) -> Net-(C112-Pad2)
- J13 pad 1: (no net) -> Net-(C111-Pad2)
- J14 pad 1: Net-(C37-Pad2) -> Net-(C109-Pad2)
- J2 pad 10: Net-(C37-Pad2) -> Net-(C107-Pad2)
- J2 pad 12: Net-(C37-Pad2) -> Net-(C107-Pad2)
- J2 pad 14: Net-(C37-Pad2) -> Net-(C107-Pad2)
- J2 pad 16: Net-(C37-Pad2) -> Net-(C107-Pad2)
- J2 pad 18: Net-(C37-Pad2) -> Net-(C107-Pad2)
- J2 pad 2: Net-(C37-Pad2) -> Net-(C107-Pad2)
- J2 pad 20: Net-(C37-Pad2) -> Net-(C107-Pad2)
- J2 pad 22: Net-(C37-Pad2) -> Net-(C107-Pad2)
- J2 pad 24: Net-(C37-Pad2) -> Net-(C107-Pad2)
- J2 pad 26: Net-(C37-Pad2) -> Net-(C107-Pad2)
- J2 pad 28: Net-(C37-Pad2) -> Net-(C107-Pad2)
- J2 pad 30: Net-(C37-Pad2) -> Net-(C107-Pad2)
- J2 pad 32: Net-(C37-Pad2) -> Net-(C107-Pad2)
- J2 pad 4: Net-(C37-Pad2) -> Net-(C107-Pad2)
- J2 pad 6: Net-(C37-Pad2) -> Net-(C107-Pad2)
- J2 pad 8: Net-(C37-Pad2) -> Net-(C107-Pad2)
- J4 pad 1: (no net) -> Net-(C114-Pad1)
- J5 pad 1: (no net) -> Net-(C113-Pad1)
- J6 pad 1: Net-(C100-Pad2) -> Net-(C110-Pad1)
- J7 pad 1: Net-(C37-Pad2) -> Net-(C109-Pad2)
- J9 pad 1: Net-(C100-Pad2) -> Net-(C110-Pad1)
- L18 pad 1: Net-(C37-Pad2) -> Net-(C107-Pad2)
- U2 pad 10: Net-(C37-Pad2) -> Net-(C107-Pad2)
- U3 pad 10: Net-(C37-Pad2) -> Net-(C107-Pad2)
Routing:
- net Net-(C37-Pad2): track 287.1 -> 0.00 mm
- net Net-(C107-Pad2): track 0.00 -> 282.3 mm
- net Net-(C110-Pad1): track 0.00 -> 54.6 mm
- net Net-(C109-Pad2): track 0.00 -> 50.2 mm
- net Net-(C107-Pad1): track 55.6 -> 75.2 mm
- net RLYPWR: track 75.1 -> 65.5 mm
- net Net-(C112-Pad2): track 0.00 -> 7.54 mm
- net GND: track 36.6 -> 30.1 mm
- net Net-(C114-Pad1): track 0.00 -> 6.46 mm
- net Net-(C113-Pad1): track 0.00 -> 6.45 mm
- net Net-(C111-Pad2): track 0.00 -> 5.15 mm
- net Net-(C108-Pad1): track 77.6 -> 82.0 mm
- net SCL: track 163.2 -> 159.1 mm
- net Net-(C100-Pad2): track 373.7 -> 369.6 mm
- net EXTPWR: track 79.9 -> 83.3 mm
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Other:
- board size 101 x 100 mm -> 99.1 x 99.6 mm

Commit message: JLCPCB submitted RelayControl version
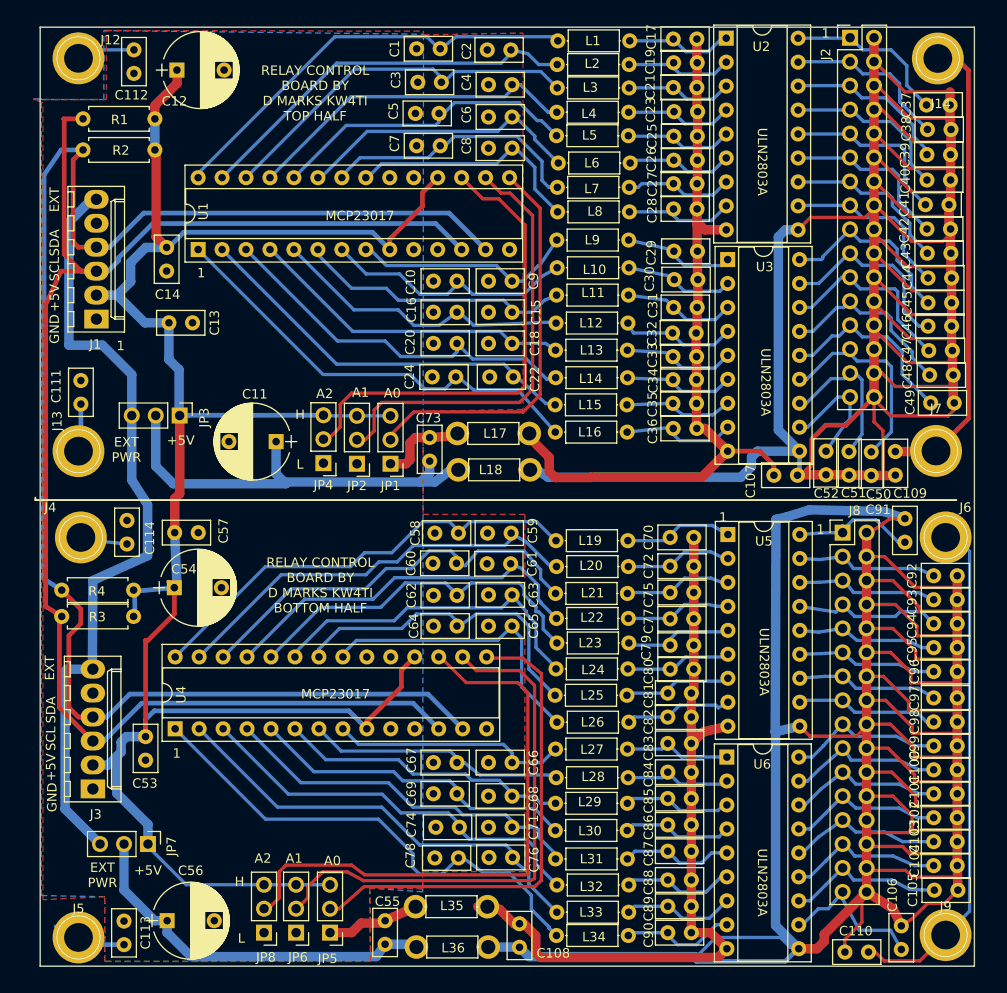
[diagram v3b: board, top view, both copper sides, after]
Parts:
- moved L18 17.3 mm to (103.8, 96.6)
- moved L17 7.22 mm to (96.1, 92.8)
- moved L9 1.07 mm to (114.2, 72.3)
- moved L10 0.93 mm to (114.2, 75.2)
- moved C73 0.58 mm to (93.1, 93.2)
- moved L11 0.56 mm to (114.2, 78.1)
- moved L16 0.52 mm to (114.1, 92.6)
- moved L12 0.39 mm to (114.1, 81.1)
- moved L13 0.30 mm to (114.1, 83.9)
- moved L14 0.18 mm to (114.1, 86.8)
- moved L15 0.17 mm to (114.0, 89.7)
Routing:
- net Net-(C107-Pad2): track 282.3 -> 311.8 mm
- net RLYPWR: track 65.5 -> 46.4 mm
- net Net-(C100-Pad2): track 369.6 -> 379.7 mm
- net GND: track 30.1 -> 20.9 mm
- net Net-(C107-Pad1): track 75.2 -> 82.2 mm
- net Net-(C9-Pad1): track 22.8 -> 23.8 mm
